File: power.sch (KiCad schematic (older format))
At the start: 21 parts, among them J16 Conn_01x03, U4 LM2574-5.0V, U5 LM2574-3.3V

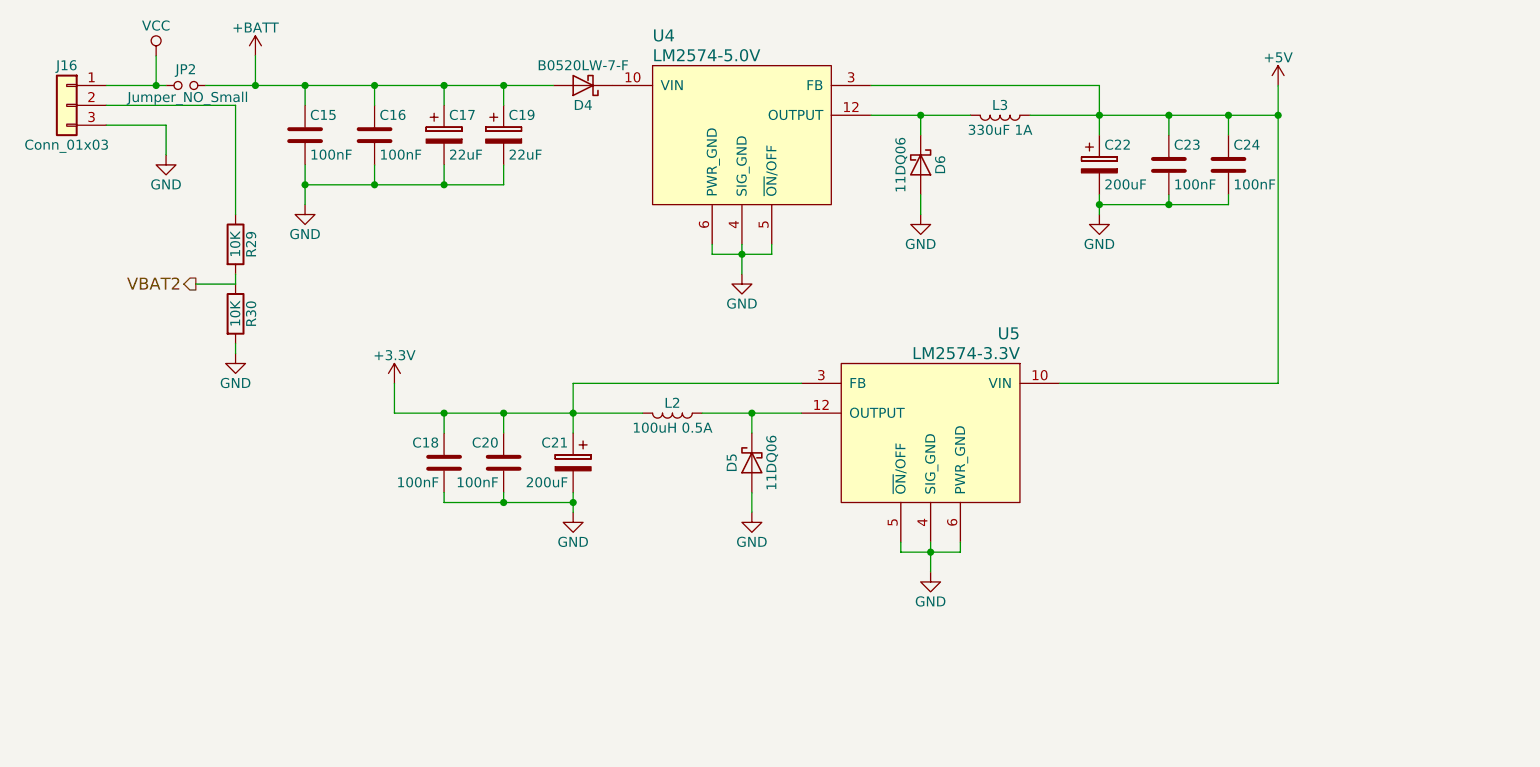
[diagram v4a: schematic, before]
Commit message: recalculated power and added new supply schem.
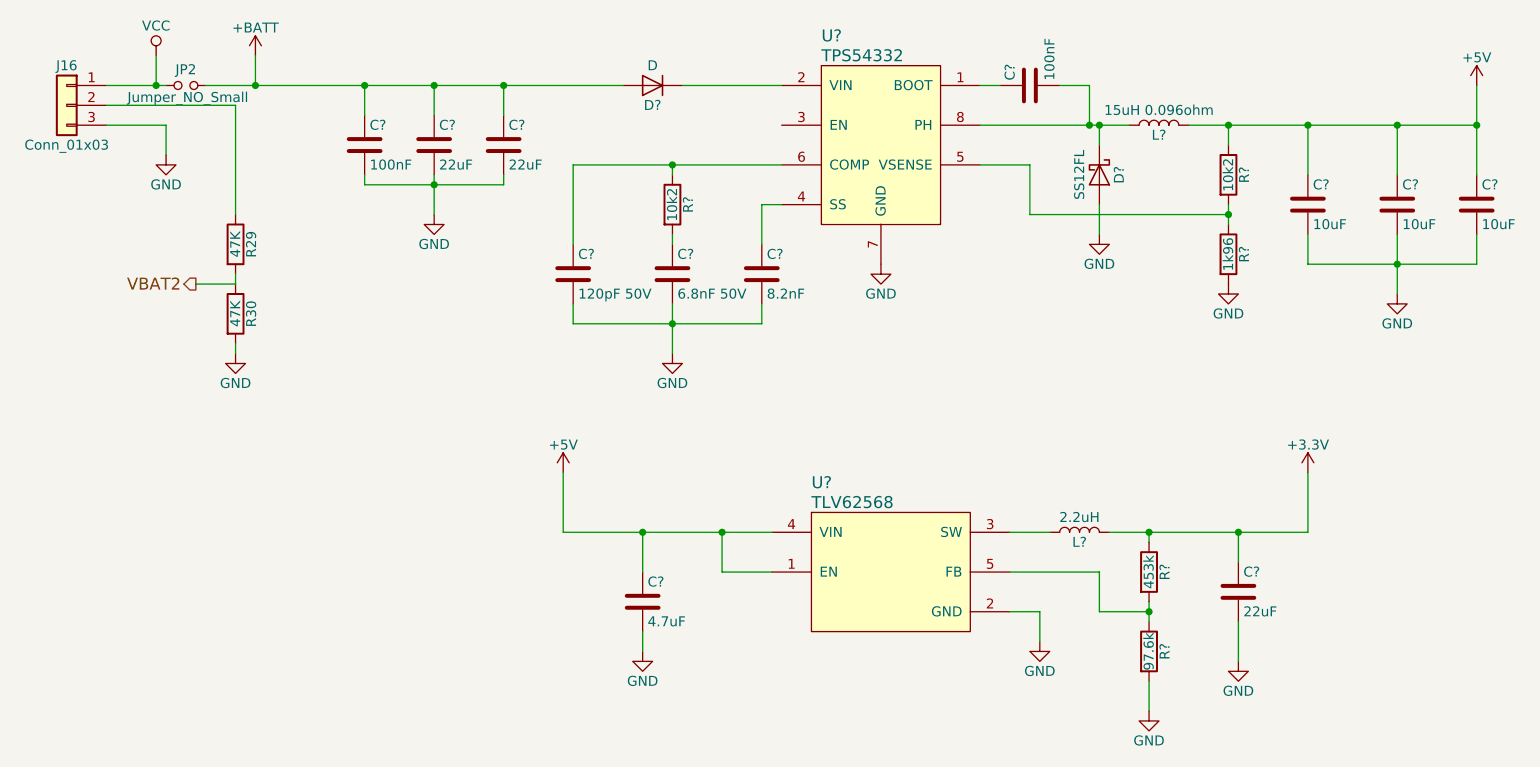
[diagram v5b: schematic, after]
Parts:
- removed C15, C16, C18, C20, C23, C24: 100nF, Capacitors_SMD:C_0805, symbol C
- removed C17, C19: 22uF, Capacitors_THT:CP_Radial_D5.0mm_P2.00mm, symbol CP
- removed C21, C22: 200uF, Capacitors_THT:CP_Radial_D5.0mm_P2.00mm, symbol CP
- removed D4: B0520LW-7-F, Diodes_SMD:D_SOD-123, symbol D_Schottky
- removed D5, D6: 11DQ06, Diodes_THT:D_DO-41_SOD81_P2.54mm_Vertical_AnodeUp, symbol D_Schottky
- removed L2: 100uH 0.5A, Inductors_THT:L_Radial_D8.7mm_P5.00mm_Fastron_07HCP, symbol L
- removed L3: 330uF 1A, Inductors_THT:L_Radial_D8.7mm_P5.00mm_Fastron_07HCP, symbol L
- removed U4: LM2574-5.0V, Housings_SOIC:SOIC-14W_7.5x9.0mm_Pitch1.27mm, symbol LM2574
- removed U5: LM2574-3.3V, Housings_SOIC:SOIC-14W_7.5x9.0mm_Pitch1.27mm, symbol LM2574
- added C? (x2): 100nF, symbol C
- added C?: 120pF 50V, symbol C
- added C?: 6.8nF 50V, symbol C
- added C?: 8.2nF, symbol C
- added C? (x3): 22uF, symbol C
- added C? (x3): 10uF, symbol C
- added C?: 4.7uF, symbol C
- added D?: D, symbol D
- added D?: SS12FL, symbol D_Schottky
- added L?: 15uH 0.096ohm, symbol L
- added L?: 2.2uH, symbol L
- added R? (x2): 10k2, symbol R
- added R?: 1k96, symbol R
- added R?: 453k, symbol R
- added R?: 97.6k, symbol R
- added U?: TPS54332, symbol TPS54332
- added U?: TLV62568, symbol TLV62568
- R29, R30: value 10K -> 47K
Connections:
- net +3V3: now also C?.1, L?.2, R?.1
- net +5V: now also C?.1, C?.1, C?.1, C?.1, L?.2, R?.1, U?.1 (EN), U?.4 (VIN)
- net +BATT: now also C?.1, C?.1, C?.1, D?.2 (A)
- net GND: now also C?.2, C?.2, C?.2, C?.2, C?.2, C?.2, C?.2, C?.2, C?.2, C?.2, C?.2, D?.2 (A), R?.2, R?.2, U?.2 (GND), U?.7 (GND), U?.9 (GND)
- new net: C?.1, U?.1 (BOOT)
- new net: D?.1 (K), U?.2 (VIN)
- new net: C?.1, U?.4 (SS)
- new net: R?.1, R?.2, U?.5 (VSENSE)
- new net: C?.1, R?.1, U?.6 (COMP)
- new net: C?.2, D?.1 (K), L?.1, U?.8 (PH)
- new net: C?.1, R?.2
- new net: L?.1, U?.3 (SW)
- new net: R?.1, R?.2, U?.5 (FB)

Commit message: pushed new psu to pcb
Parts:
- C15, C16, C17, C18, C19, C20, C21, C22, C23, C24, C30, C31: renamed from C?; footprint (none) -> Capacitors_SMD:C_0805
- D4: renamed from D?; value D -> 30V 1.5A 400mV Vf; footprint (none) -> Diodes_SMD:D_SOD-323
- D5: renamed from D?; value SS12FL -> 0.55V 1A; footprint (none) -> Diodes_SMD:D_SOD-123F
- L2, L3: renamed from L?; footprint (none) -> Inductors_SMD:L_Taiyo-Yuden_NR-60xx
- R31, R32, R33, R34, R35: renamed from R?; footprint (none) -> Resistors_SMD:R_0805
- U4: renamed from U?; footprint (none) -> Housings_SOIC:SOIC-8-1EP_3.9x4.9mm_Pitch1.27mm
- U5: renamed from U?; footprint (none) -> TO_SOT_Packages_SMD:SOT-23-5
